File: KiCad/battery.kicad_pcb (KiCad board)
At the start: 2 copper layers, 22.9 x 21.6 mm, 7 parts, among them J1 GND, J2 Conn_01x01_Male, J3 Conn_01x01_Male, U1 ATtiny, U2 LD1117S33TR_SOT223

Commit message: Use PB4 to pull T pin low instead of PB5
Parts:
- J1: value GND -> Conn_01x07_Male
- U1: value ATtiny -> ATtiny85-20SU
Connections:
- U1 pad 1: T -> Net-(U1-Pad1)
- U1 pad 3: CurrentSensor -> T
- U1 pad 6: Net-(U1-Pad6) -> CurrentSensor
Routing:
- net T: track 5.54 -> 9.43 mm
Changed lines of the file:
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@@
-(kicad_pcb (version 20171130) (host pcbnew 5.1.6-c6e7f7d~86~ubuntu18.04.1)
+(kicad_pcb (version 20171130) (host pcbnew 5.1.5+dfsg1-2build2)
   (general
     (thickness 1.6)
     (drawings 4)
-    (tracks 43)
+    (tracks 45)
     (zones 0)
     (modules 7)
@@
   (net 4 12v)
   (net 5 SCL)
-  (net 6 "Net-(U1-Pad6)")
-  (net 7 SDA)
-  (net 8 CurrentSensor)
-  (net 9 T)
+  (net 6 SDA)
+  (net 7 CurrentSensor)
+  (net 8 T)
+  (net 9 "Net-(U1-Pad1)")
   (net_class Default "This is the default net class."
     (clearance 0.2)
@@
     (add_net CurrentSensor)
     (add_net GND)
-    (add_net "Net-(U1-Pad6)")
+    (add_net "Net-(U1-Pad1)")
     (add_net SCL)
     (add_net SDA)
@@
       (effects (font (size 1 1) (thickness 0.15)))
     )
-    (fp_text value GND (at 0 17.57 90) (layer F.Fab)
+    (fp_text value Conn_01x07_Male (at 0 17.57 90) (layer F.Fab)
       (effects (font (size 1 1) (thickness 0.15)))
     )
@@
       (net 1 GND))
     (pad 5 thru_hole oval (at 0 10.16 90) (size 1.7 1.7) (drill 1) (layers *.Cu *.Mask)
-      (net 9 T))
+      (net 8 T))
     (pad 4 thru_hole oval (at 0 7.62 90) (size 1.7 1.7) (drill 1) (layers *.Cu *.Mask)
-      (net 7 SDA))
+      (net 6 SDA))
     (pad 3 thru_hole oval (at 0 5.08 90) (size 1.7 1.7) (drill 1) (layers *.Cu *.Mask)
       (net 5 SCL))
@@
       (effects (font (size 1 1) (thickness 0.15)))
     )
-    (fp_text value ATtiny (at 0 3.68) (layer F.Fab) hide
+    (fp_text value ATtiny85-20SU (at 0 3.68) (layer F.Fab) hide
       (effects (font (size 1 1) (thickness 0.15)))
     )
@@
       (net 5 SCL))
     (pad 6 smd rect (at 3.65 0.635 180) (size 1.7 0.65) (layers F.Cu F.Paste F.Mask)
-      (net 6 "Net-(U1-Pad6)"))
+      (net 7 CurrentSensor))
     (pad 5 smd rect (at 3.65 1.905 180) (size 1.7 0.65) (layers F.Cu F.Paste F.Mask)
-      (net 7 SDA))
+      (net 6 SDA))
     (pad 4 smd rect (at -3.65 1.905 180) (size 1.7 0.65) (layers F.Cu F.Paste F.Mask)
       (net 1 GND))
     (pad 3 smd rect (at -3.65 0.635 180) (size 1.7 0.65) (layers F.Cu F.Paste F.Mask)
-      (net 8 CurrentSensor))
+      (net 8 T))
     (pad 2 smd rect (at -3.65 -0.635 180) (size 1.7 0.65) (layers F.Cu F.Paste F.Mask)
       (net 3 VBatSensor))
     (pad 1 smd rect (at -3.65 -1.905 180) (size 1.7 0.65) (layers F.Cu F.Paste F.Mask)
-      (net 9 T))
+      (net 9 "Net-(U1-Pad1)"))
     (model ${KISYS3DMOD}/Package_SO.3dshapes/SOIJ-8_5.3x5.3mm_P1.27mm.wrl
       (at (xyz 0 0 0))
@@
   (segment (start 140.96 95.25) (end 141.035001 95.325001) (width 0.25) (layer F.Cu) (net 5))
   (segment (start 139.86 95.25) (end 140.96 95.25) (width 0.25) (layer F.Cu) (net 5))
-  (segment (start 139.86 92.71) (end 142.24 92.71) (width 0.25) (layer F.Cu) (net 7))
-  (segment (start 143.51 93.98) (end 143.51 101.6) (width 0.25) (layer F.Cu) (net 7))
-  (segment (start 142.24 92.71) (end 143.51 93.98) (width 0.25) (layer F.Cu) (net 7))
-  (segment (start 147.16 100.49) (end 146.05 101.6) (width 0.25) (layer F.Cu) (net 9))
-  (segment (start 147.16 96.52) (end 147.16 100.49) (width 0.25) (layer F.Cu) (net 9))
+  (segment (start 139.86 92.71) (end 142.24 92.71) (width 0.25) (layer F.Cu) (net 6))
+  (segment (start 143.51 93.98) (end 143.51 101.6) (width 0.25) (layer F.Cu) (net 6))
+  (segment (start 142.24 92.71) (end 143.51 93.98) (width 0.25) (layer F.Cu) (net 6))
+  (segment (start 145.200001 100.750001) (end 146.05 101.6) (width 0.25) (layer F.Cu) (net 8))
+  (segment (start 145.200001 94.839999) (end 145.200001 100.750001) (width 0.25) (layer F.Cu) (net 8))
+  (segment (start 146.06 93.98) (end 145.200001 94.839999) (width 0.25) (layer F.Cu) (net 8))
+  (segment (start 147.16 93.98) (end 146.06 93.98) (width 0.25) (layer F.Cu) (net 8))
   (zone (net 1) (net_name GND) (layer F.Cu) (hatch edge 0.508)
     (connect_pads (clearance 0))

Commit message: better pcb
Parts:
- moved J3 14.0 mm to (151.1, 97.8)
- moved J2 14.0 mm to (135.9, 97.8)
- moved U2 1.41 mm to (141.0, 87.6)
- moved U1 0.64 mm to (143.5, 95.2)
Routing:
- net 12v: track 39.7 -> 22.1 mm
- net GND: track 42.6 -> 32.1 mm
- net 3.3v: track 7.54 -> 9.59 mm
- net VBatSensor: track 9.17 -> 9.99 mm
- net SDA: track 11.8 -> 11.2 mm
- net T: track 9.43 -> 8.80 mm
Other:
- board size 22.9 x 21.6 mm -> 19 x 21 mm

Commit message: Update PCB before manufacturing
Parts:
- removed J3: Conn_01x01_Male, Connector_Pin:Pin_D1.4mm_L8.5mm_W2.8mm_FlatFork
- added C1: 22uF, Capacitor_SMD:C_0805_2012Metric, F.Cu at (154.9, 106.3)
- added C2: 22uF, Capacitor_SMD:C_0805_2012Metric, F.Cu at (165.1, 105.1)
- added R3: 10k, Resistor_SMD:R_0402_1005Metric, F.Cu at (153.2, 113.7)
- added R4: 10k, Resistor_SMD:R_0402_1005Metric, F.Cu at (153.2, 109.9)
- J1: value Conn_01x07_Male -> Conn_01x06_Male; footprint Connector_PinHeader_2.54mm:PinHeader_1x07_P2.54mm_Vertical -> Connector_PinHeader_2.54mm:PinHeader_1x06_P2.54mm_Horizontal
- J2: value Conn_01x01_Male -> Conn_01x02_Male; footprint Connector_Pin:Pin_D1.4mm_L8.5mm_W2.8mm_FlatFork -> Connector_PinHeader_2.54mm:PinHeader_1x02_P2.54mm_Vertical
- R1: value 3K -> 3.3K; footprint Parts:R_1206_3216Metric_Pad1.42x1.75mm_HandSolder -> Resistor_SMD:R_0402_1005Metric
- R2: value 9.1K -> 10K; footprint Parts:R_1206_3216Metric_Pad1.42x1.75mm_HandSolder -> Resistor_SMD:R_0402_1005Metric
- moved J1 32.5 mm to (163.8, 118.1), turned to 270 degrees
- moved J2 29.2 mm to (165.1, 97.8)
- moved R2 25.6 mm to (153.2, 112.4), turned to 0 degrees
- moved U2 25.0 mm to (160.3, 103.5), turned to 90 degrees
- moved R1 23.7 mm to (153.2, 111.1), turned to 0 degrees
- moved U1 23.5 mm to (160.2, 111.8), turned to 0 degrees
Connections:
- J1 pad 2: 12v -> SDA
- J1 pad 4: SDA -> T
- J1 pad 5: T -> CurrentSensor
- J2 pad 1: 12v -> 3.3v
- U1 pad 1: Net-(U1-Pad1) -> R
- U1 pad 3: T -> T_C
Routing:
- net 3.3v: track 9.59 -> 31.4 mm
- net 12v: track 22.1 -> 38.0 mm, vias 0 -> 2
- net CurrentSensor: track 0.00 -> 12.5 mm, vias 0 -> 1
- net GND: track 32.1 -> 39.7 mm, vias 0 -> 4
- net VBatSensor: track 9.99 -> 4.13 mm
- net SDA: track 11.2 -> 6.61 mm
- net T_C: track 0.00 -> 3.39 mm
- net T: track 8.80 -> 5.90 mm
- net R: track 0.00 -> 2.86 mm
- net SCL: track 7.62 -> 10.2 mm
- added copper zone on B.Cu, net GND
- removed copper zone on F.Cu, net 12v
- removed copper zone on F.Cu, net GND
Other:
- board outline removed
- board text added: "iam SMBUS Board V1"

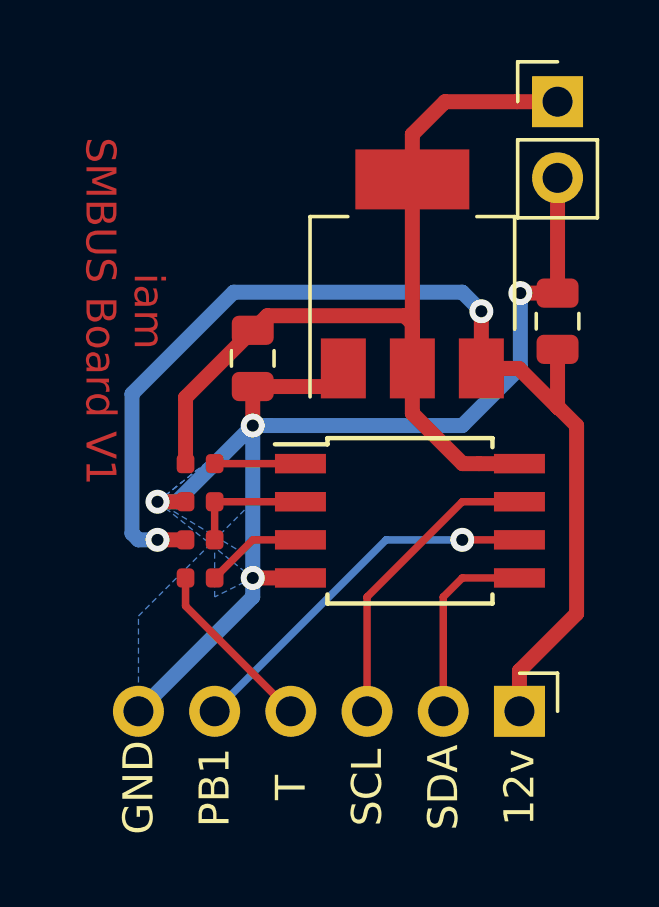
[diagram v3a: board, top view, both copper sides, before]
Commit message: R1 bq3060
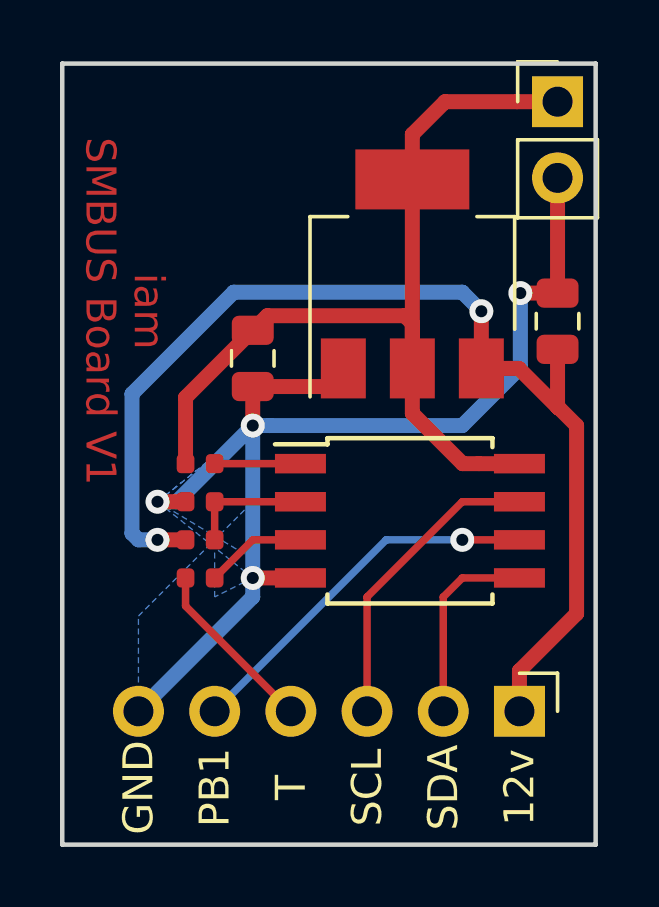
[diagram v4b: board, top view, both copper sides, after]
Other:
- board outline added: 17.8 x 26 mm
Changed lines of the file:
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@@
   )
   (setup
-    (last_trace_width 0.5)
+    (last_trace_width 0.25)
     (user_trace_width 0.25)
     (user_trace_width 0.5)
@@
     (effects (font (size 1 1) (thickness 0.15)))
   )
-  (gr_line (start 148.59 122.555) (end 148.59 96.52) (layer F.Fab) (width 0.15))
-  (gr_line (start 166.37 122.555) (end 148.59 122.555) (layer F.Fab) (width 0.15))
-  (gr_line (start 166.37 96.52) (end 166.37 122.555) (layer F.Fab) (width 0.15))
-  (gr_line (start 148.59 96.52) (end 166.37 96.52) (layer F.Fab) (width 0.15))
+  (gr_line (start 148.59 122.555) (end 148.59 96.52) (layer Edge.Cuts) (width 0.15))
+  (gr_line (start 166.37 122.555) (end 148.59 122.555) (layer Edge.Cuts) (width 0.15))
+  (gr_line (start 166.37 96.52) (end 166.37 122.555) (layer Edge.Cuts) (width 0.15))
+  (gr_line (start 148.59 96.52) (end 166.37 96.52) (layer Edge.Cuts) (width 0.15))
   (segment (start 156.53 113.665) (end 154.94 113.665) (width 0.5) (layer F.Cu) (net 1))
   (segment (start 154.94 113.665) (end 154.94 113.665) (width 0.5) (layer F.Cu) (net 1))
